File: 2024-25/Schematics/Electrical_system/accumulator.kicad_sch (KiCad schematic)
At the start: 13 parts, among them K1 GV24 1BAX, K3 P115 BDA, K4 GV24 1BAX, U12 IMD, U16 Battery Pack, U2 BMS, U3 RSB, U5 Volt_indic, U6 precharge

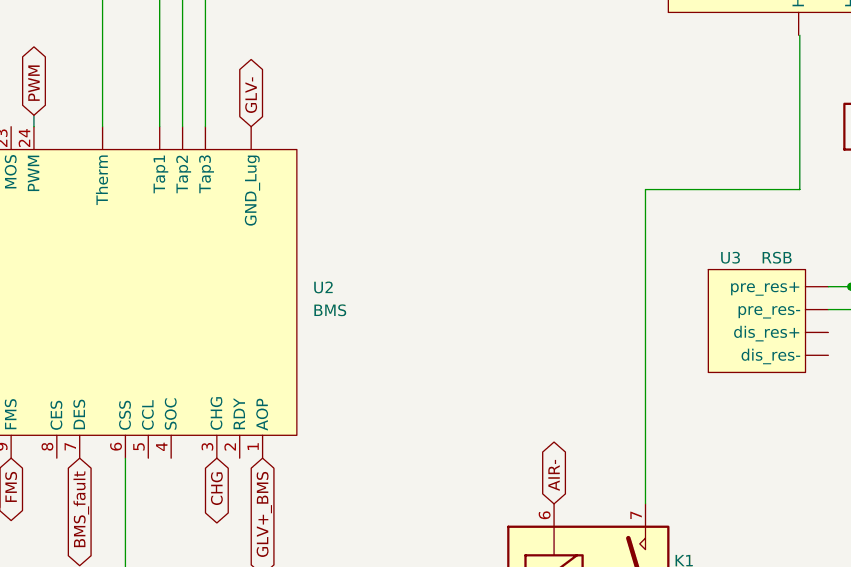
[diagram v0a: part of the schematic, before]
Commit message: added current sensor
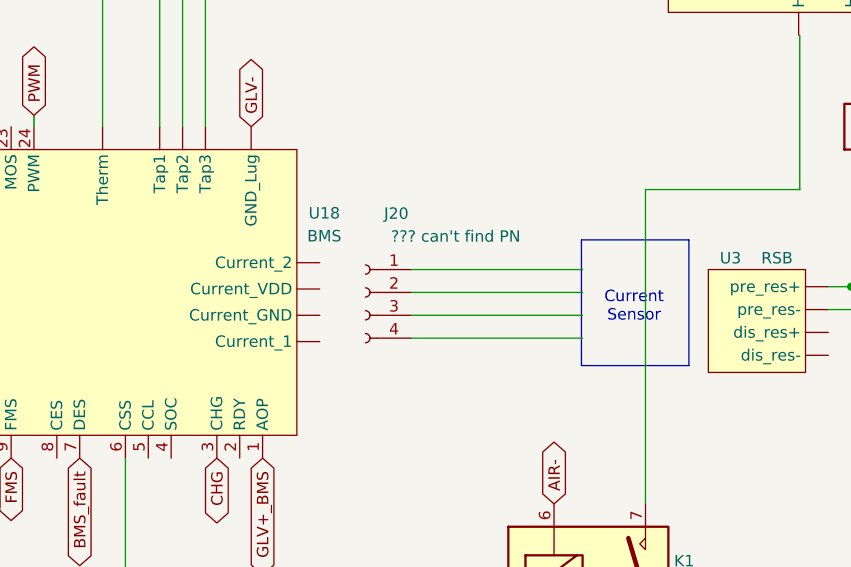
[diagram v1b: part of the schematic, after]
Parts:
- removed U2: BMS, symbol FSAE:BMS
- added J20: ??? can't find PN, symbol Connector:Conn_01x04_Socket
- added U18: BMS, symbol FSAE:BMS
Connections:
- net BMS_fault: now also U18.7 (DES)
- net CANH: now also U18.18 (C1H)
- net CANL: now also U18.19 (C1L)
- net CANS: now also U18.17 (C1S)
- net CHG: now also U18.3 (CHG)
- net CONTROL_PILOT: now also U18.13 (MPI1)
- net FMS: now also U18.9 (FMS)
- net FPC: now also U18.10 (FPC)
- net GLV+_BMS: now also U18.1 (AOP)
- net GNDPWR: now also U18. (Therm), U18.11 (GND), U18.12 (GND)
- net PROX_DET: now also U18.14 (MPI2)
- net PWM: now also U18.24 (PWM)
- net charge_safe: now also U18.6 (CSS)
- net at U3. (pre_res-): now also K3.7, K3.8
- new net: U16. (Therm), U18. (Therm) (x4)
- now unconnected: U16. (Therm), U16. (Therm), U16. (Therm)
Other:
- note added: "Current Sensor"
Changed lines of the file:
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@@
 	(wire
 		(pts
-			(xy 153.035 100.33) (xy 153.035 74.93)
-		)
-		(stroke
-			(width 0)
-			(type default)
-		)
-	)
-	(wire
-		(pts
 			(xy 141.605 83.82) (xy 141.605 100.33)
 		)
@@
 	(wire
 		(pts
-			(xy 147.955 100.33) (xy 147.955 80.01)
+			(xy 153.035 100.33) (xy 153.035 74.93)
 		)
 		(stroke
@@
 	(wire
 		(pts
+			(xy 175.895 123.825) (xy 194.945 123.825)
+		)
+		(stroke
+			(width 0)
+			(type default)
+		)
+	)
+	(wire
+		(pts
 			(xy 191.77 157.48) (xy 191.77 160.02)
 		)
@@
 	(wire
 		(pts
+			(xy 175.895 121.285) (xy 194.945 121.285)
+		)
+		(stroke
+			(width 0)
+			(type default)
+		)
+	)
+	(wire
+		(pts
 			(xy 274.32 165.1) (xy 251.46 165.1)
 		)
@@
 	(wire
 		(pts
+			(xy 147.955 100.33) (xy 147.955 80.01)
+		)
+		(stroke
+			(width 0)
+			(type default)
+		)
+	)
+	(wire
+		(pts
+			(xy 175.895 116.205) (xy 194.945 116.205)
+		)
+		(stroke
+			(width 0)
+			(type default)
+		)
+	)
+	(wire
+		(pts
 			(xy 201.93 107.315) (xy 201.93 142.24)
 		)
@@
 	(wire
 		(pts
+			(xy 175.895 118.745) (xy 194.945 118.745)
+		)
+		(stroke
+			(width 0)
+			(type default)
+		)
+	)
+	(wire
+		(pts
 			(xy 126.365 202.565) (xy 126.365 203.835)
 		)
@@
 		)
 	)
+	(rectangle
+		(start 194.818 112.903)
+		(end 206.756 126.873)
+		(stroke
+			(width 0)
+			(type default)
+		)
+		(fill
+			(type none)
+		)
+	)
 	(text "All GLV- wires are tied to Chassis"
 		(exclude_from_sim no)
@@
 		)
 	)
+	(text "Current\nSensor"
+		(exclude_from_sim no)
+		(at 200.66 120.396 0)
+		(effects
+			(font
+				(size 1.27 1.27)
+			)
+		)
+	)
 	(text "crimps: SXH-001T-P0.6N\n"
 		(exclude_from_sim no)
@@
 		(dnp no)
 		(fields_autoplaced yes)
-		(property "Reference" "U2"
-			(at 164.973 118.237 90)
+		(property "Reference" "U18"
+			(at 166.243 109.9468 90)
 			(effects
 				(font
 					(size 1.27 1.27)
 				)
-				(justify right)
 			)
 		)
 		(property "Value" "BMS"
-			(at 164.973 120.777 90)
+			(at 166.243 112.4868 90)
 			(effects
 				(font
 					(size 1.27 1.27)
 				)
-				(justify right)
 			)
 		)
 		(property "Footprint" ""
-			(at 164.973 118.237 0)
+			(at 164.211 99.187 0)
 			(effects
 				(font
@@
 		)
 		(property "Datasheet" ""
-			(at 164.973 118.237 0)
+			(at 164.211 99.187 0)
 			(effects
 				(font
@@
 		)
 		(property "Description" ""
-			(at 164.973 118.237 0)
+			(at 164.211 99.187 0)
 			(effects
 				(font
@@
 			)
 		)
-		(pin ""
+		(pin "1"
 		)
-		(pin ""
+		(pin "21"
 		)
-		(pin ""
+		(pin "22"
 		)
-		(pin ""
+		(pin "23"
 		)
 		(pin ""
 		)
-		(pin "1"
+		(pin "18"
 		)
-		(pin "10"
+		(pin "19"
 		)
-		(pin "11"
+		(pin "16"
 		)
-		(pin "12"
+		(pin "17"
 		)
-		(pin "13"
+		(pin ""
 		)
-		(pin "14"
+		(pin "24"
 		)
-		(pin "15"
+		(pin "3"
 		)
-		(pin "16"
+		(pin "4"
 		)
-		(pin "17"
+		(pin "5"
 		)
-		(pin "18"
+		(pin "6"
 		)
-		(pin "19"
+		(pin "7"
 		)
-		(pin "2"
+		(pin "8"
 		)
-		(pin "20"
+		(pin "9"
 		)
-		(pin "21"
+		(pin "12"
 		)
-		(pin "22"
+		(pin "13"
 		)
-		(pin "23"
+		(pin "14"
 		)
-		(pin "24"
+		(pin "15"
 		)
-		(pin "3"
+		(pin ""
 		)
-		(pin "4"
+		(pin ""
 		)
-		(pin "5"
+		(pin ""
 		)
-		(pin "6"
+		(pin ""
 		)
-		(pin "7"
+		(pin "10"
 		)
-		(pin "8"
+		(pin "11"
 		)
-		(pin "9"
+		(pin ""
+		)
+		(pin ""
+		)
+		(pin "2"
+		)
+		(pin "20"
+		)
+		(pin ""
 		)
 		(instances
-			(project "accumulator"
-				(path "/257053c5-9a9c-4e07-83c1-3de2ea3e3dc0"
-					(reference "U2")
-					(unit 1)
-				)
-			)
 			(project "Electrical_system"
 				(path "/9fd63cb4-0e42-461f-94fb-36140af5f720/9a7d5ecd-e5aa-4565-80da-5476528c3ffe"
-					(reference "U2")
+					(reference "U18")
 					(unit 1)
 				)
@@
 					(unit 1)
 				)
+			)
+		)
+	)
+	(symbol
+		(lib_id "Connector:Conn_01x04_Socket")
+		(at 170.815 118.745 0)
+		(mirror y)
+		(unit 1)
+		(exclude_from_sim no)
+		(in_bom yes)
+		(on_board yes)
+		(dnp no)
+		(property "Reference" "J20"
+			(at 174.244 109.982 0)
+			(effects
+				(font
+					(size 1.27 1.27)
+				)
+			)
+		)
+		(property "Value" "??? can't find PN"
+			(at 180.848 112.522 0)
+			(effects
+				(font
+					(size 1.27 1.27)
+				)
+			)
+		)
+		(property "Footprint" ""
+			(at 170.815 118.745 0)
+			(effects
+				(font
+					(size 1.27 1.27)
+				)
+				(hide yes)
+			)
+		)
+		(property "Datasheet" "~"
+			(at 170.815 118.745 0)
+			(effects
+				(font
+					(size 1.27 1.27)
+				)
+				(hide yes)
+			)
+		)
+		(property "Description" "Generic connector, single row, 01x04, script generated"
+			(at 170.815 118.745 0)
+			(effects
+				(font
+					(size 1.27 1.27)
+				)
+				(hide yes)
+			)
+		)
+		(pin "1"
+		)
+		(pin "2"
+		)
+		(pin "4"
+		)
+		(pin "3"
+		)
+		(instances
+			(project "Electrical_system"
+				(path "/9fd63cb4-0e42-461f-94fb-36140af5f720/9a7d5ecd-e5aa-4565-80da-5476528c3ffe"
+					(reference "J20")
+					(unit 1)
+				)

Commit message: updates
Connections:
- net at U3. (pre_res-): now also K3.7, K3.8
- net at U16. (Therm): no longer U18. (Therm)
- new net: U16. (Therm), U18. (Therm) (x4)
- now unconnected: U16. (Therm), U16. (Therm), U16. (Therm)
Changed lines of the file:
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@@
 	(wire
 		(pts
-			(xy 95.25 209.55) (xy 95.25 218.44)
+			(xy 146.05 209.55) (xy 146.05 218.44)
 		)
 		(stroke
@@
 	(global_label "charge_on"
 		(shape input)
-		(at 95.25 209.55 90)
-		(fields_autoplaced yes)
-		(effects
-			(font
-				(size 1.27 1.27)
-			)
-			(justify left)
-		)
-		(property "Intersheetrefs" "${INTERSHEET_REFS}"
-			(at 95.25 196.8888 90)
+		(at 146.05 209.55 90)
+		(fields_autoplaced yes)
+		(effects
+			(font
+				(size 1.27 1.27)
+			)
+			(justify left)
+		)
+		(property "Intersheetrefs" "${INTERSHEET_REFS}"
+			(at 146.05 196.8888 90)
 			(effects
 				(font
@@
 	(hierarchical_label "charge_on"
 		(shape input)
-		(at 95.25 218.44 270)
-		(fields_autoplaced yes)
-		(effects
+		(at 146.05 218.44 270)
+		(fields_autoplaced yes)
+		(effects

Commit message: ESF updates
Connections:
- net AIR+_en: now also U6.7 (AIR+_en); no longer U6.3 (AIR+_en)
- net CHG: now also U6.3 (CHG); no longer U6.1 (CHG)
- net GLV+: now also U6.1 (VCC); no longer U6.7 (VCC)
- net GNDPWR: now also U6.2 (GND); no longer U6.5 (GND)
- net PreAIR_en: now also U6.6 (Pre_en); no longer U6.4 (PreAIR_en)
- net SDC2: now also U6.5 (SDCin); no longer U6.6 (SDCin)
- net charge_on: now also U6.4 (charge_on); no longer U6.2 (charge_on)
- net HV-_preair: now reaches K1.7, K1.8
- net HV-_preair: now also U6. (HV-_preair)
- net HV+_preair: now reaches U3. (pre_res-)
- net HV+_preair: now also F2.2, K4.7, K4.8, U6. (HV-_preair)
- net at U16. (Therm): no longer U18. (Therm)
- net PostAIR+ renamed HV+_postair
- net HV+_postair: now also U6. (HV-_preair)
- net PostAIR- renamed HV-_postair
- net HV-_postair: now also U6. (HV-_preair)
- new net: U16. (Therm), U18. (Therm) (x4)
- new net PC_error: U6.8 (PC_error)
- now unconnected: U16. (Therm), U16. (Therm), U16. (Therm)

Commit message: ESF fixes + energy meter updates
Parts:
- added F3: Fuse, symbol Device:Fuse
- added R4: RCH50S15001JS06, symbol Device:R_US
- added U19: DS18B20-PAR, Package_TO_SOT_THT:TO-92_Inline, symbol Sensor_Temperature:DS18B20-PAR
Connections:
- net at U16. (Therm): no longer U18. (Therm)
- net HV+_postair renamed PostAIR+
- net PostAIR+: now also F3.1, R4.2
- net HV-_postair renamed PostAIR-
- new net: U16. (Therm), U18. (Therm) (x4)
- new net HV+_bamo: F3.2
- new net HV+_tsmp: R4.1
- new net temp_GND: U19.1 (GND)
- new net temp_sense: U19.2 (DQ)
- now unconnected: U16. (Therm), U16. (Therm), U16. (Therm)
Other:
- note added: "HV+ TSMP resistor & fuse for low current HV wire placed here reduced ampacity rule"
- moved on the sheet: D1, U5

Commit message: integration cleanups
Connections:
- net at U16. (Therm): no longer U18. (Therm)
- net HV+_bamo renamed HV+_TSAL
- new net: U16. (Therm), U18. (Therm) (x4)
- now unconnected: U16. (Therm), U16. (Therm), U16. (Therm)
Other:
- note added: "HV+ TSMP resistor & fuse for TSAL HV wire placed here reduced ampacity rule discharge HV+ unfused"
- note removed: "HV+ TSMP resistor & fuse for low current HV wire placed here reduced ampacity rule"
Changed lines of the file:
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@@
+	)
+	(junction
+		(at 281.305 165.1)
+		(diameter 0)
+		(color 0 0 0 0)
 	)
 	(junction
@@
 	(wire
 		(pts
+			(xy 281.305 165.1) (xy 286.385 165.1)
+		)
+		(stroke
+			(width 0)
+			(type default)
+			(color 204 102 0 1)
+		)
+	)
+	(wire
+		(pts
 			(xy 153.035 74.93) (xy 201.93 74.93)
 		)
@@
 	(wire
 		(pts
-			(xy 274.32 165.1) (xy 286.385 165.1)
+			(xy 274.32 165.1) (xy 281.305 165.1)
 		)
 		(stroke
@@
 			(width 0)
 			(type default)
+		)
+	)
+	(wire
+		(pts
+			(xy 281.305 165.1) (xy 281.305 218.44)
+		)
+		(stroke
+			(width 0)
+			(type default)
+			(color 204 102 0 1)
 		)
 	)
@@
 		)
 	)
-	(text "HV+ TSMP resistor &\nfuse for low current HV wire\nplaced here reduced ampacity rule"
+	(text "HV+ TSMP resistor &\nfuse for TSAL HV wire\nplaced here reduced ampacity rule\ndischarge HV+ unfused"
 		(exclude_from_sim no)
-		(at 298.831 190.5 0)
+		(at 301.498 190.5 0)
 		(effects
 			(font
@@
 	)
 	(hierarchical_label "HV+_tsmp"
-		(shape input)
+		(shape output)
 		(at 290.83 218.44 270)
 		(fields_autoplaced yes)
@@
 		)
 	)
-	(hierarchical_label "HV+_bamo"
-		(shape input)
+	(hierarchical_label "HV+_TSAL"
+		(shape output)
 		(at 286.385 218.44 270)
 		(fields_autoplaced yes)
@@
 		(fields_autoplaced yes)
 		(effects
+			(font
+				(size 1.27 1.27)
+			)
+			(justify right)
+		)
+	)
+	(hierarchical_label "HV+_discharge"
+		(shape output)
+		(at 281.305 218.44 270)
+		(fields_autoplaced yes)
+		(effects

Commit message: harness updates
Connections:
- net at U16. (Therm): no longer U18. (Therm)
- net HV+_TSAL renamed HV+_Emeter
- new net: U16. (Therm), U18. (Therm) (x4)
- now unconnected: U16. (Therm), U16. (Therm), U16. (Therm)
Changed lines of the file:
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@@
+	)
+	(junction
+		(at 286.385 194.945)
+		(diameter 0)
+		(color 0 0 0 0)
 	)
 	(junction
@@
 	(wire
 		(pts
+			(xy 283.845 194.945) (xy 286.385 194.945)
+		)
+		(stroke
+			(width 0)
+			(type default)
+			(color 204 102 0 1)
+		)
+	)
+	(wire
+		(pts
 			(xy 224.79 104.14) (xy 224.79 118.11)
 		)
@@
 	(wire
 		(pts
+			(xy 283.845 194.945) (xy 283.845 218.44)
+		)
+		(stroke
+			(width 0)
+			(type default)
+			(color 204 102 0 1)
+		)
+	)
+	(wire
+		(pts
 			(xy 127 59.69) (xy 127.635 59.69)
 		)
@@
 	(wire
 		(pts
-			(xy 286.385 192.405) (xy 286.385 218.44)
-		)
-		(stroke
-			(width 0)
-			(type default)
-			(color 204 102 0 1)
-		)
-	)
-	(wire
-		(pts
 			(xy 201.93 107.315) (xy 201.93 133.985)
 		)
@@
 	(wire
 		(pts
+			(xy 286.385 194.945) (xy 286.385 218.44)
+		)
+		(stroke
+			(width 0)
+			(type default)
+			(color 204 102 0 1)
+		)
+	)
+	(wire
+		(pts
 			(xy 127 63.5) (xy 127.635 63.5)
 		)
@@
 			(width 0)
 			(type default)
+		)
+	)
+	(wire
+		(pts
+			(xy 286.385 192.405) (xy 286.385 194.945)
+		)
+		(stroke
+			(width 0)
+			(type default)
+			(color 204 102 0 1)
 		)
 	)
@@
 		(fields_autoplaced yes)
 		(effects
+			(font
+				(size 1.27 1.27)
+			)
+			(justify right)
+		)
+	)
+	(hierarchical_label "HV+_Emeter"
+		(shape output)
+		(at 283.845 218.44 270)
+		(fields_autoplaced yes)
+		(effects

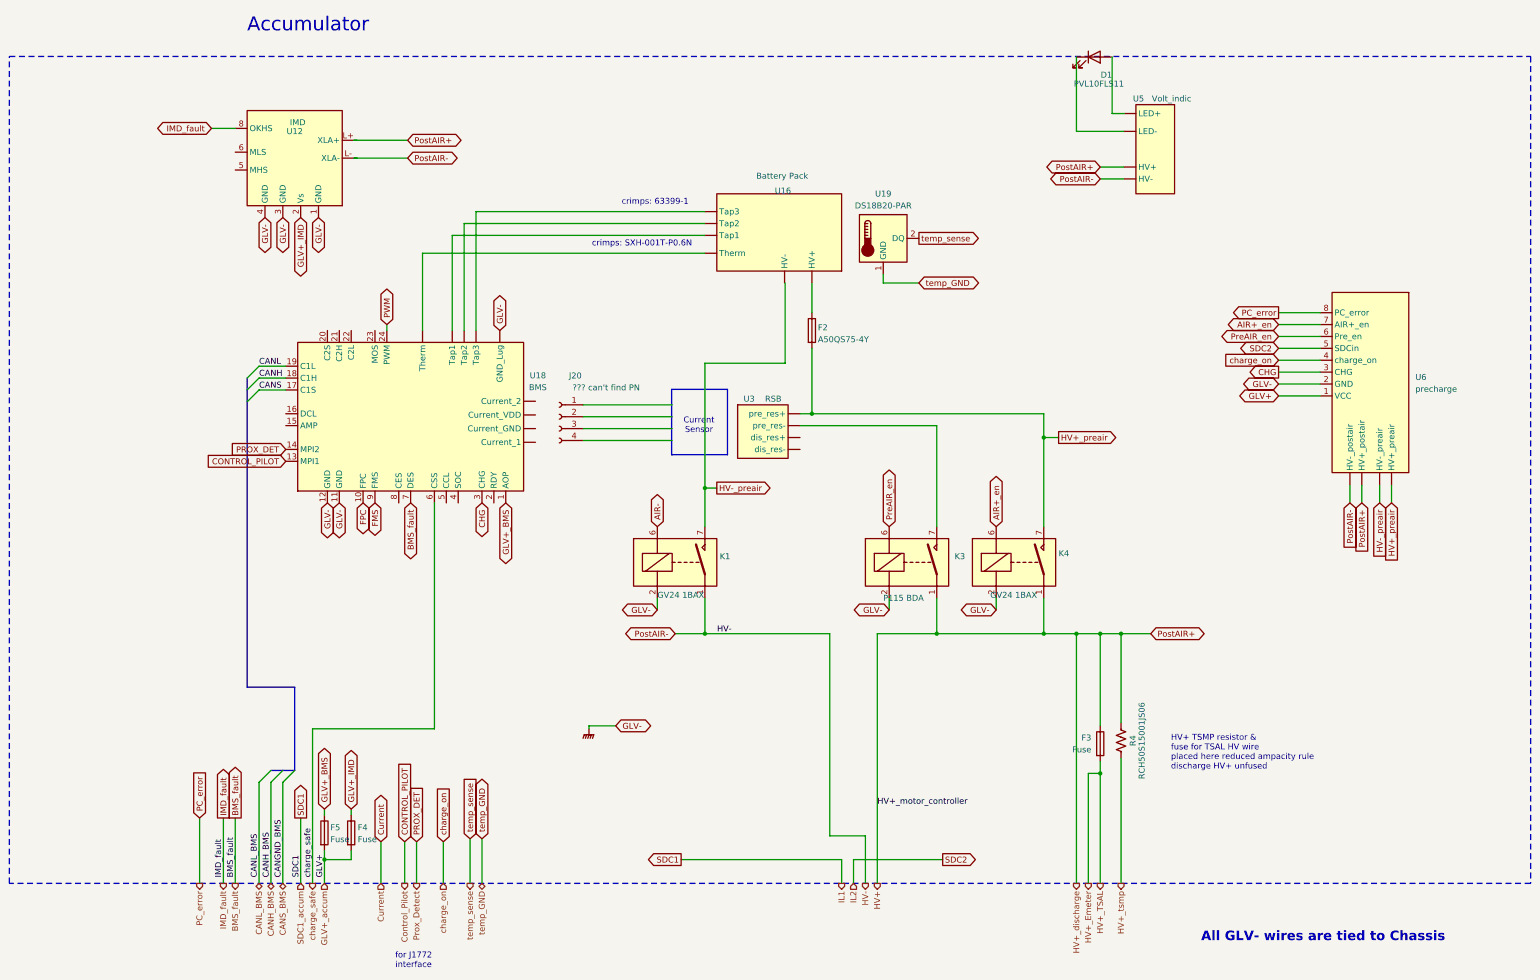
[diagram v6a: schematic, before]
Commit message: fixed precharge wiring
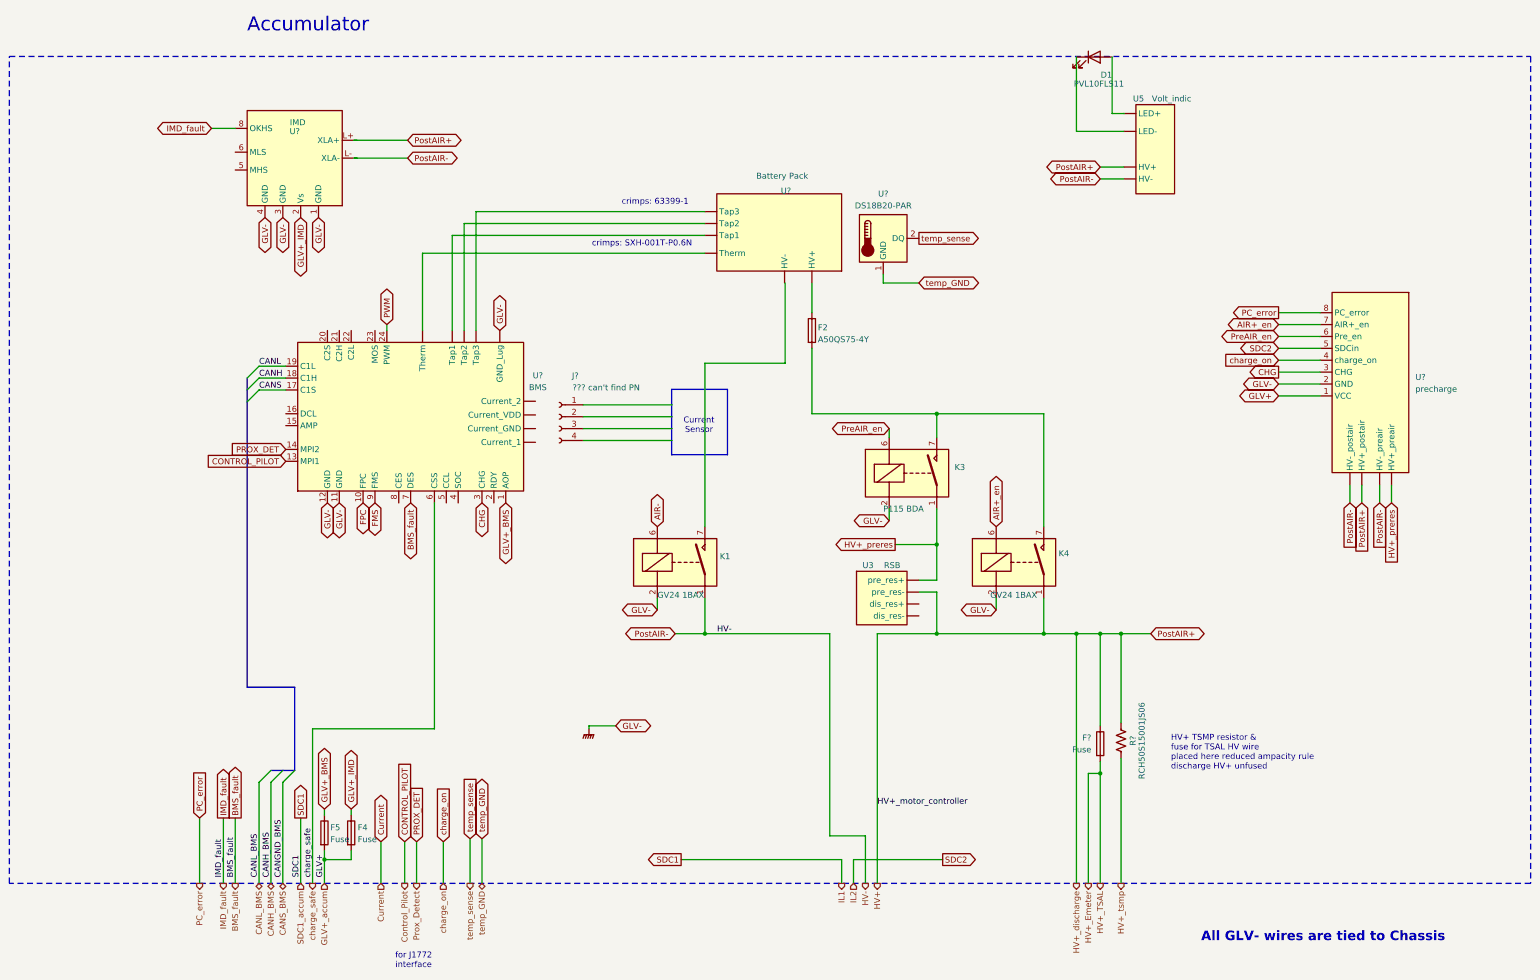
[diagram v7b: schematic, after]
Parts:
- renumbered F3 to F?, J20 to J?, R4 to R?, U18 to U?, U19 to U?, U16 to U?, U12 to U?, U6 to U?
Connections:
- net PostAIR+: now also U3. (dis_res-); no longer K3.1, K3.14
- net at K3.7, K3.8: now also F2.2, K4.7, K4.8; no longer U3. (pre_res-)
- net at U?. (Tap3): no longer U?. (Therm)
- removed net HV+_preair: F2.2, K4.7, K4.8, U3. (pre_res-), U?. (HV-_preair)
- net HV-_preair: no longer names the net of K1.7, K1.8
- net HV-_preair: no longer U?. (HV-_preair)
- new net: U?. (GND_Lug), U?. (Tap3) (x4)
- new net HV+_preres: K3.1, K3.14, U3. (dis_res-), U?. (HV-_postair)
- now unconnected: U?. (Therm), U?. (Therm), U?. (Therm)
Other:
- moved on the sheet: K3, U3
